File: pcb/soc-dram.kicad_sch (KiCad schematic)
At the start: 0 parts

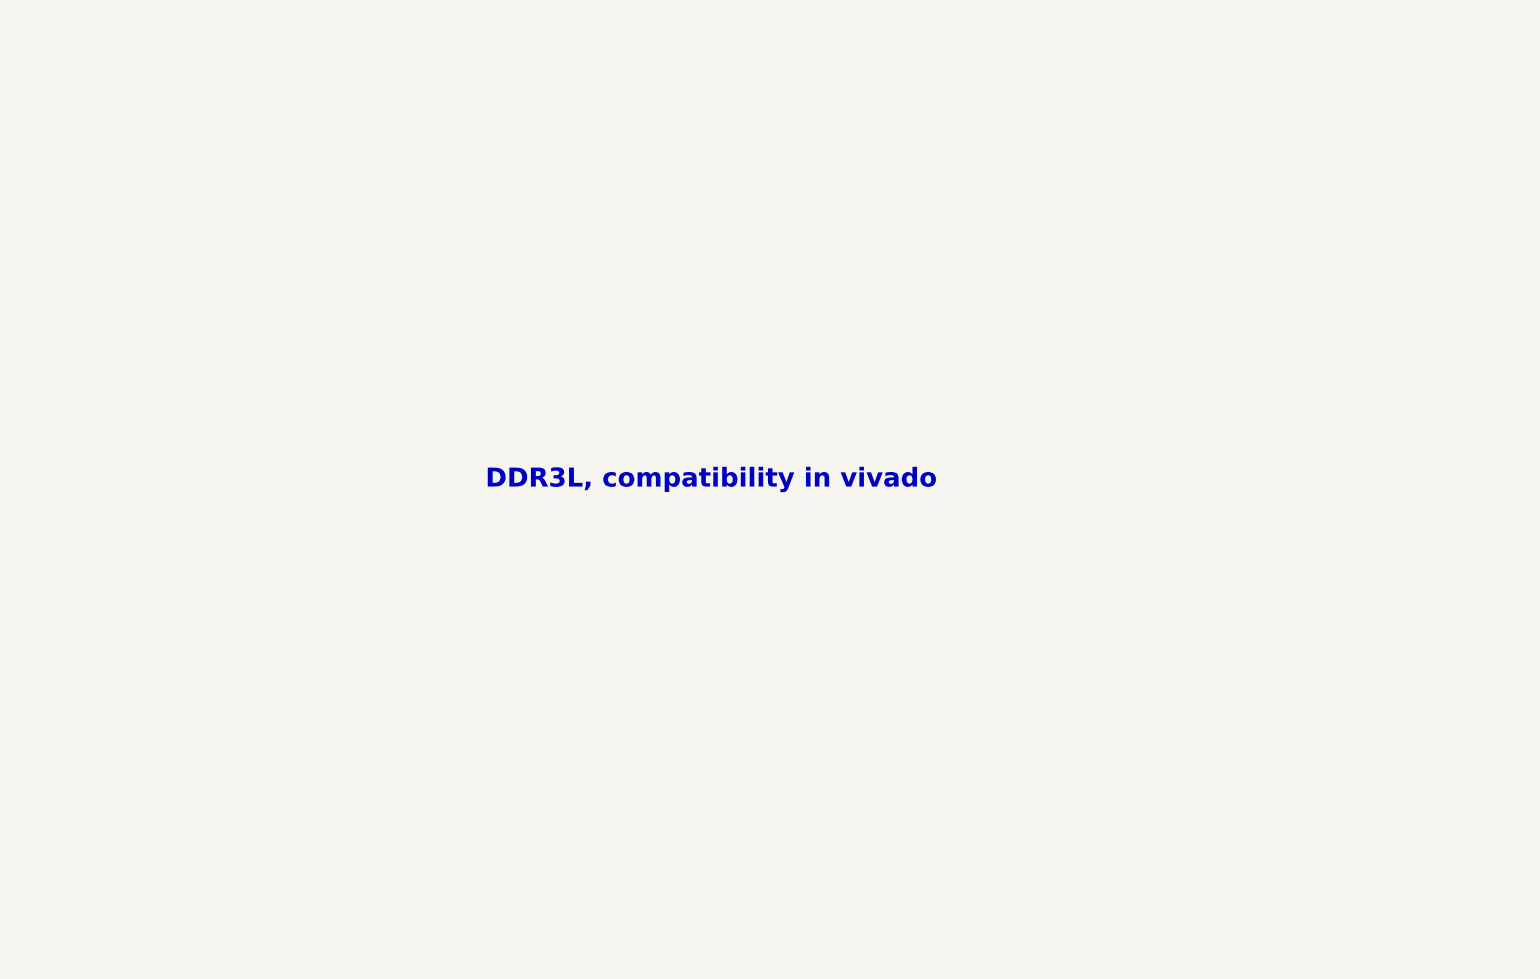
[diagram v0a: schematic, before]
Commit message: added ddr3l
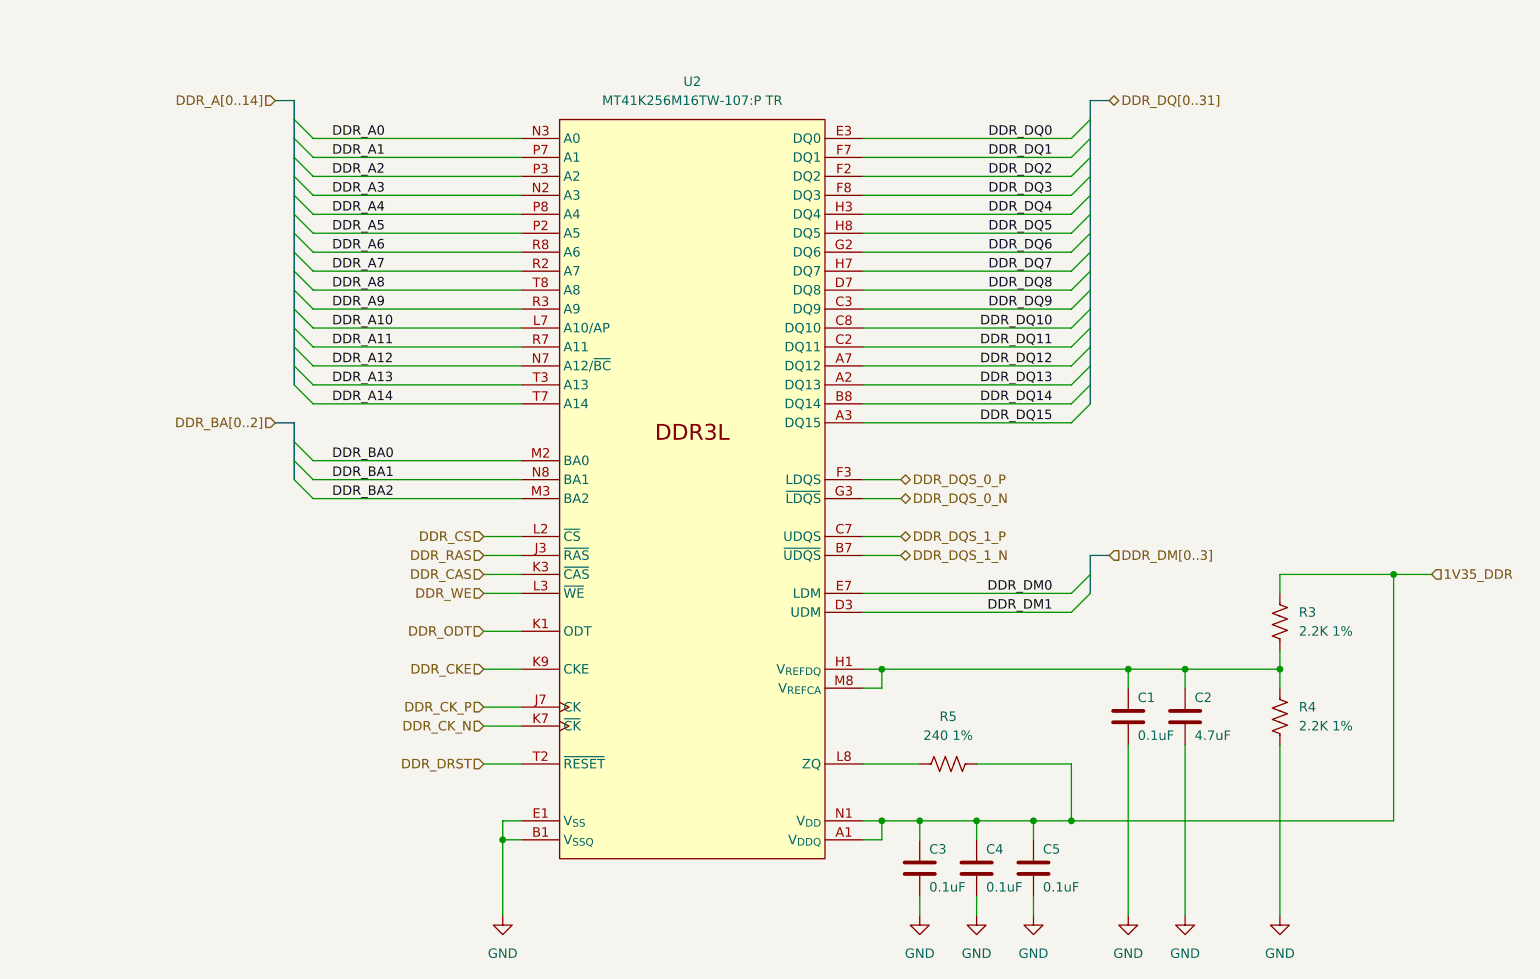
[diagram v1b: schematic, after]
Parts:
- added C1, C3, C4, C5: 0.1uF, Capacitor_SMD:C_0402_1005Metric, symbol library:C
- added C2: 4.7uF, Capacitor_SMD:C_0603_1608Metric, symbol library:C
- added R3, R4: 2.2K 1%, Resistor_SMD:R_0402_1005Metric, symbol library:R_US
- added R5: 240 1%, Resistor_SMD:R_0402_1005Metric, symbol library:R_US
- added U2: MT41K256M16TW-107:P TR, Package_BGA:Micron_FBGA-96_7.5x13.5mm_Layout9x16_P0.8mm, symbol library:MT41K256M16LY
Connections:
- new net: C1.2, C2.1, R3.2, R4.1, U2.H1 (V_{REFDQ}), U2.M8 (V_{REFCA})
- new net: R5.1, U2.L8 (ZQ)
- new net 1V35_DDR: C3.2, C4.2, C5.2, R3.1, R5.2, U2.A1 (V_{DDQ}), U2.A8 (V_{DDQ}), U2.B2 (V_{DD}), U2.C1 (V_{DDQ}), U2.C9 (V_{DDQ}), U2.D2 (V_{DDQ}), U2.D9 (V_{DD}), U2.E9 (V_{DDQ}), U2.F1 (V_{DDQ}), U2.G7 (V_{DD}), U2.H2 (V_{DDQ}), U2.H9 (V_{DDQ}), U2.K2 (V_{DD}), U2.K8 (V_{DD}), U2.N1 (V_{DD}), U2.N9 (V_{DD}), U2.R1 (V_{DD}), U2.R9 (V_{DD})
- new net DDR_A0: U2.N3 (A0)
- new net DDR_A1: U2.P7 (A1)
- new net DDR_A10: U2.L7 (A10/AP)
- new net DDR_A11: U2.R7 (A11)
- new net DDR_A12: U2.N7 (A12/~{BC})
- new net DDR_A13: U2.T3 (A13)
- new net DDR_A14: U2.T7 (A14)
- new net DDR_A2: U2.P3 (A2)
- new net DDR_A3: U2.N2 (A3)
- new net DDR_A4: U2.P8 (A4)
- new net DDR_A5: U2.P2 (A5)
- new net DDR_A6: U2.R8 (A6)
- new net DDR_A7: U2.R2 (A7)
- new net DDR_A8: U2.T8 (A8)
- new net DDR_A9: U2.R3 (A9)
- new net DDR_BA0: U2.M2 (BA0)
- new net DDR_BA1: U2.N8 (BA1)
- new net DDR_BA2: U2.M3 (BA2)
- new net DDR_CAS: U2.K3 (~{CAS})
- new net DDR_CKE: U2.K9 (CKE)
- new net DDR_CK_N: U2.K7 (~{CK})
- new net DDR_CK_P: U2.J7 (CK)
- new net DDR_CS: U2.L2 (~{CS})
- new net DDR_DM0: U2.E7 (LDM)
- new net DDR_DM1: U2.D3 (UDM)
- new net DDR_DQ0: U2.E3 (DQ0)
- new net DDR_DQ1: U2.F7 (DQ1)
- new net DDR_DQ10: U2.C8 (DQ10)
- new net DDR_DQ11: U2.C2 (DQ11)
- new net DDR_DQ12: U2.A7 (DQ12)
- new net DDR_DQ13: U2.A2 (DQ13)
- new net DDR_DQ14: U2.B8 (DQ14)
- new net DDR_DQ15: U2.A3 (DQ15)
- new net DDR_DQ2: U2.F2 (DQ2)
- new net DDR_DQ3: U2.F8 (DQ3)
- new net DDR_DQ4: U2.H3 (DQ4)
- new net DDR_DQ5: U2.H8 (DQ5)
- new net DDR_DQ6: U2.G2 (DQ6)
- new net DDR_DQ7: U2.H7 (DQ7)
- new net DDR_DQ8: U2.D7 (DQ8)
- new net DDR_DQ9: U2.C3 (DQ9)
- new net DDR_DQS_0_N: U2.G3 (~{LDQS})
- new net DDR_DQS_0_P: U2.F3 (LDQS)
- new net DDR_DQS_1_N: U2.B7 (~{UDQS})
- new net DDR_DQS_1_P: U2.C7 (UDQS)
- new net DDR_DRST: U2.T2 (~{RESET})
- new net DDR_ODT: U2.K1 (ODT)
- new net DDR_RAS: U2.J3 (~{RAS})
- new net DDR_WE: U2.L3 (~{WE})
- new net GND: C1.1, C2.2, C3.1, C4.1, C5.1, R4.2, U2.A9 (V_{SS}), U2.B1 (V_{SSQ}), U2.B3 (V_{SS}), U2.B9 (V_{SSQ}), U2.D1 (V_{SSQ}), U2.D8 (V_{SSQ}), U2.E1 (V_{SS}), U2.E2 (V_{SSQ}), U2.E8 (V_{SSQ}), U2.F9 (V_{SSQ}), U2.G1 (V_{SSQ}), U2.G8 (V_{SS}), U2.G9 (V_{SSQ}), U2.J2 (V_{SS}), U2.J8 (V_{SS}), U2.M1 (V_{SS}), U2.M9 (V_{SS}), U2.P1 (V_{SS}), U2.P9 (V_{SS}), U2.T1 (V_{SS}), U2.T9 (V_{SS})
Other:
- note removed: "DDR3L, compatibility in vivado"

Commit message: add eth phy
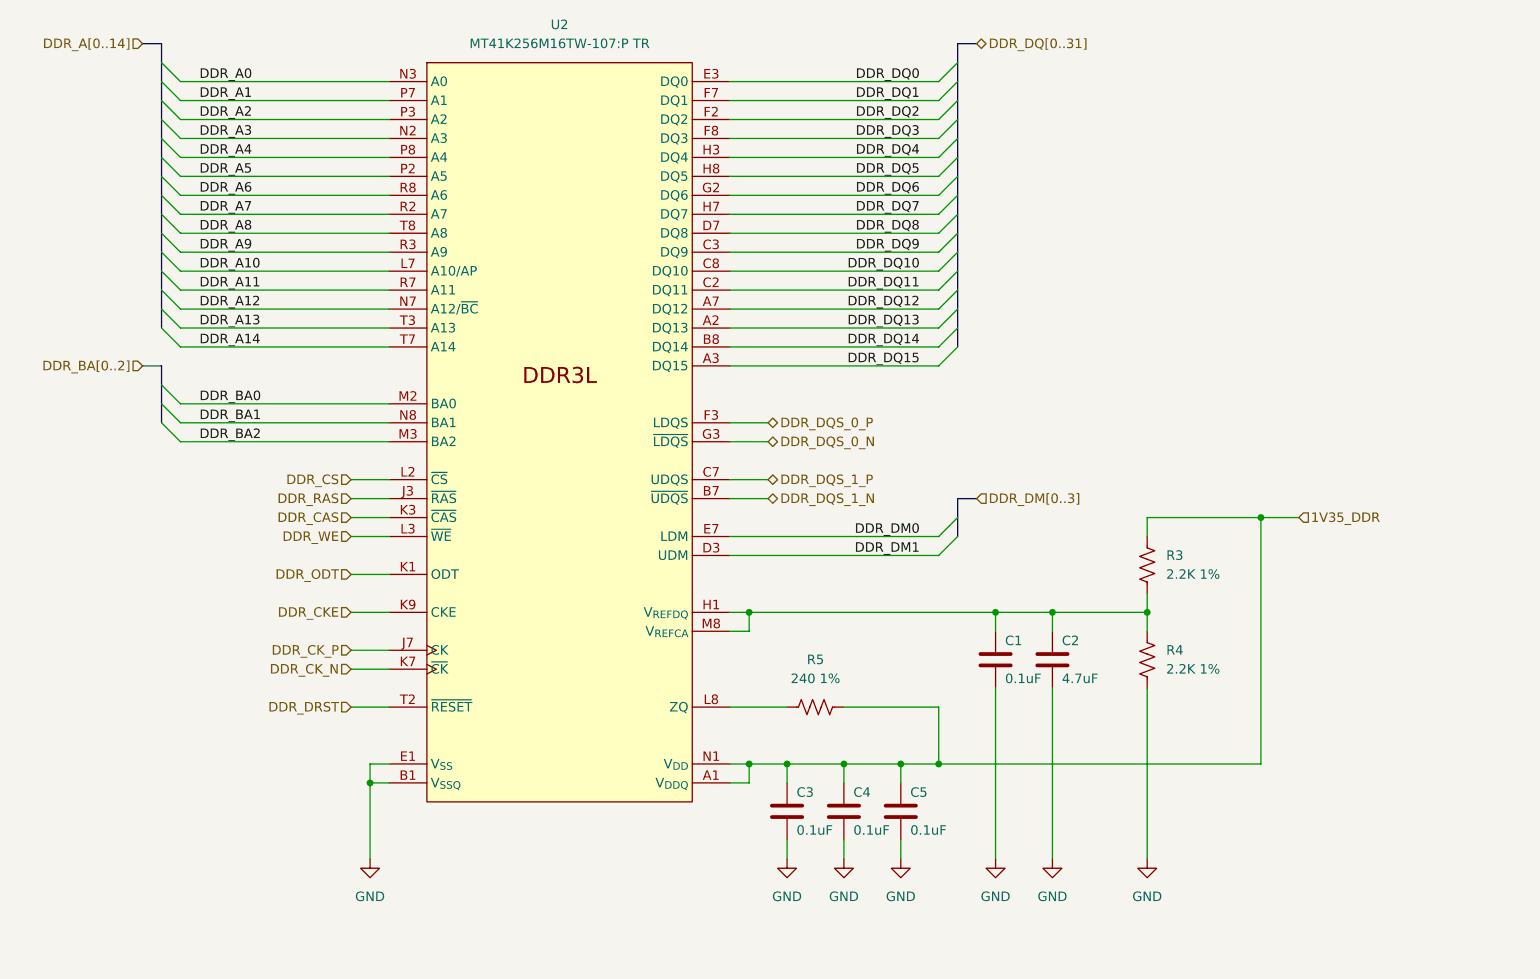
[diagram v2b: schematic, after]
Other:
- moved on the sheet: C1, C2, C3, C4, C5, R3, R4, R5, U2

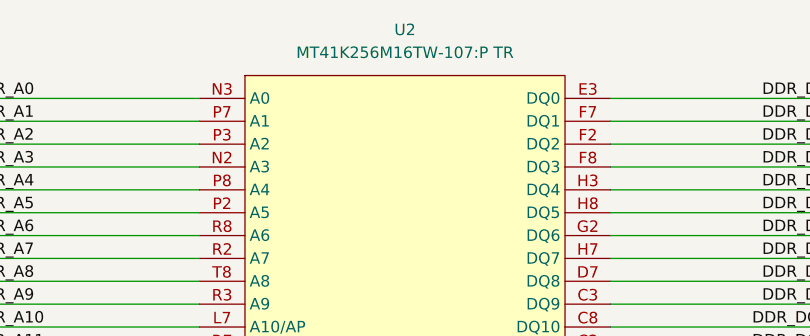
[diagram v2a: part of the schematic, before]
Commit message: phy and debug ffc conn
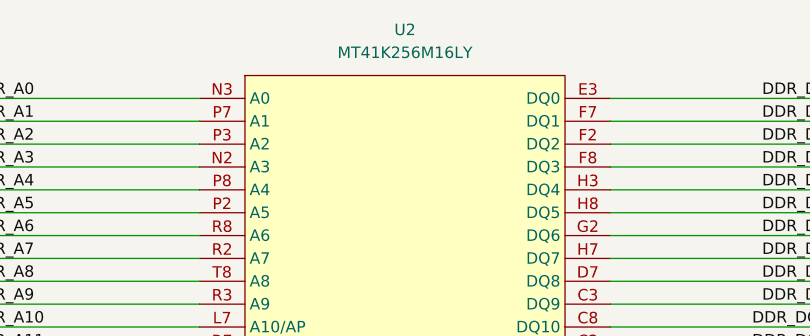
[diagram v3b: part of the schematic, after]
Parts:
- U2: value MT41K256M16TW-107:P TR -> MT41K256M16LY; Manufacturer Micron Technology Inc. -> (none); Manufacturer Product Number MT41K256M16TW-107:P TR -> (none); Part Description IC DRAM 4GBIT PAR 96FBGA -> (none)
